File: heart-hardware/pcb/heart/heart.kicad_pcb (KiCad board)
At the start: 4 copper layers, 47.6 x 45.2 mm, 66 parts, among them J1 3V0, J2 DIO, J3 CLK, J5 TOUCH_KEY, SW1 SW_SPDT, U1 STM32L031F6Px, U2 TCA6416APWR, U3 LIS3DH, U4 Holtek-Semicon-BS812A-1

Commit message: Component pacement v1
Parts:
- moved C5 2.13 mm to (42.5, 66.2)
- moved C4 2.12 mm to (42.5, 67.2)
- moved R21 2.10 mm to (42.5, 65.2)
- moved C2 1.97 mm to (57.5, 69.0), turned to 0 degrees
- moved R23 1.45 mm to (57.5, 66.0)
- moved R22 1.33 mm to (57.5, 67.0)
- moved C10 1.25 mm to (54.0, 89.5)
- moved C11 1.23 mm to (46.0, 89.5)
- moved R26 1.10 mm to (54.0, 86.0), turned to 180 degrees
- moved R25 1.00 mm to (54.0, 85.0)
- moved C8 0.90 mm to (46.0, 85.0)
- moved C9 0.90 mm to (46.0, 86.0), turned to 180 degrees
- moved C3 0.53 mm to (57.5, 68.0), turned to 180 degrees
- moved C6 0.35 mm to (57.5, 74.0)
- moved C7 0.33 mm to (57.5, 73.0)

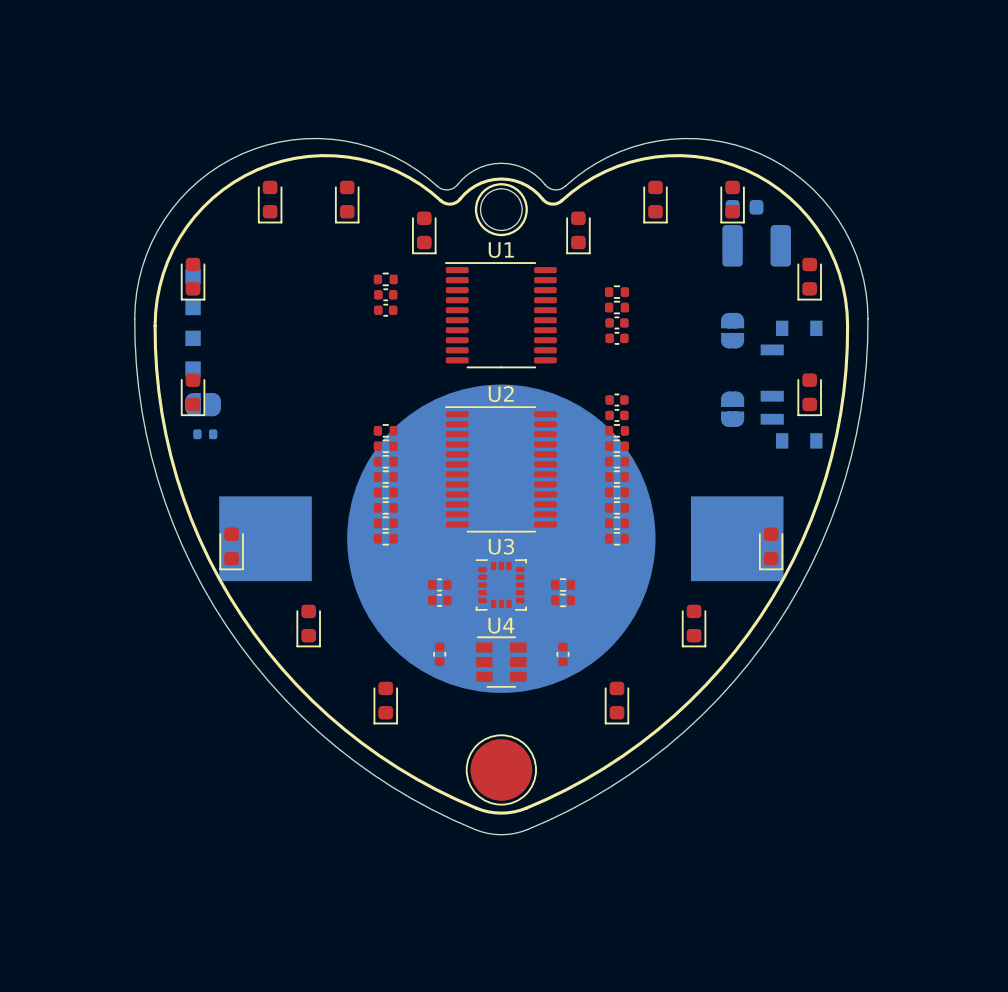
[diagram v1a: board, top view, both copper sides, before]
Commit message: Start routing traces
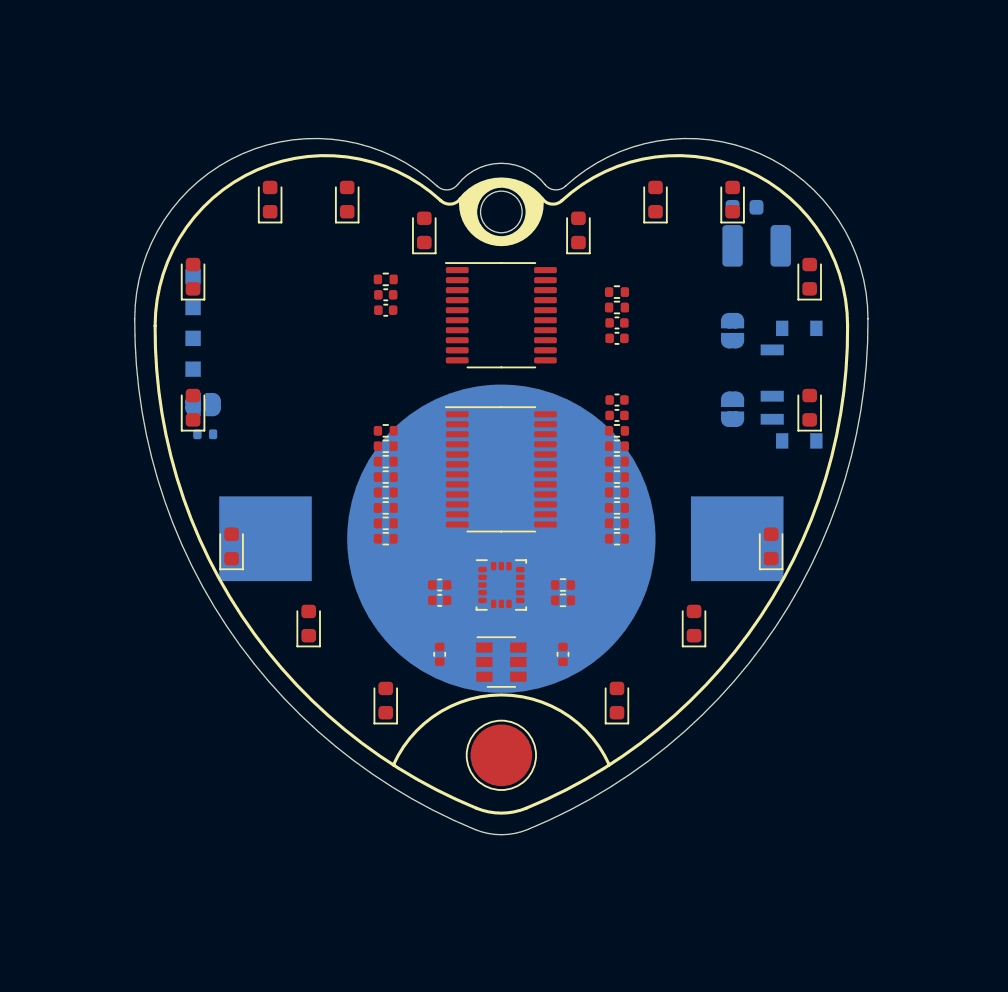
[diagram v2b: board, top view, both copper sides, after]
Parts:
- moved D11 1.00 mm to (70.0, 73.5)
- moved D4 1.00 mm to (30.0, 73.5)
- moved J5 0.95 mm to (50.0, 96.0)
- moved REF** 0.15 mm to (50.0, 60.8)
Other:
- board text removed: "E"
- board text removed: "K"
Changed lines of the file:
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@@
   (general
     (thickness 1.6)
-    (drawings 45)
+    (drawings 42)
     (tracks 0)
     (zones 0)
@@
     (pad_to_mask_clearance 0)
     (aux_axis_origin 0 0)
-    (visible_elements 7FFF7F7F)
+    (visible_elements 7FFEFF1F)
     (pcbplotparams
       (layerselection 0x010fc_ffffffff)
@@
   )
   (module MountingHole:MountingHole_2.7mm (layer F.Cu)
-    (at 50 60.65)
+    (at 50 60.8)
     (descr "Mounting Hole 2.7mm, no annular")
     (tags "mounting hole 2.7mm no annular")
@@
   )
   (module TestPoint:TestPoint_Pad_D4.0mm (layer F.Cu)
-    (at 50 97)
+    (at 50 96.05)
     (descr "SMD pad as test Point, diameter 4.0mm")
     (tags "test point SMD pad")
@@
     (tags SOT-23-6)
     (attr smd)
-    (fp_text reference U4 (at -0.01506 -2.33426) (layer F.SilkS)
+    (fp_text reference U4 (at -0.01506 -2.33426) (layer F.SilkS) hide
       (effects (font (size 1 1) (thickness 0.15)))
     )
@@
   )
   (module LED_SMD:LED_0603_1608Metric (layer F.Cu)
-    (at 30 72.5 90)
+    (at 30 73.5 90)
     (descr "LED SMD 0603 (1608 Metric), square (rectangular) end terminal, IPC_7351 nominal, (Body size source: http://www.tortai-tech.com/upload/download/2011102023233369053.pdf), generated with kicad-footprint-generator")
     (tags LED)
@@
   )
   (module LED_SMD:LED_0603_1608Metric (layer F.Cu)
-    (at 70 72.5 90)
+    (at 70 73.5 90)
     (descr "LED SMD 0603 (1608 Metric), square (rectangular) end terminal, IPC_7351 nominal, (Body size source: http://www.tortai-tech.com/upload/download/2011102023233369053.pdf), generated with kicad-footprint-generator")
     (tags LED)
@@
     (tags "LGA NoLead")
     (attr smd)
-    (fp_text reference U3 (at 0 -2.45) (layer F.SilkS)
+    (fp_text reference U3 (at 0 -2.45) (layer F.SilkS) hide
       (effects (font (size 1 1) (thickness 0.15)))
     )
@@
     (tags "TSSOP SO")
     (attr smd)
-    (fp_text reference U2 (at 0 -4.85) (layer F.SilkS)
+    (fp_text reference U2 (at 0 -4.85) (layer F.SilkS) hide
       (effects (font (size 1 1) (thickness 0.15)))
     )
@@
     (tags "TSSOP SO")
     (attr smd)
-    (fp_text reference U1 (at 0 -4.2) (layer F.SilkS)
+    (fp_text reference U1 (at 0 -4.2) (layer F.SilkS) hide
       (effects (font (size 1 1) (thickness 0.15)))
     )
@@
       ))
   )
-  (gr_text K (at 50.4 98.1) (layer B.SilkS)
-    (effects (font (size 0.75 0.75) (thickness 0.15)) (justify mirror))
-  )
-  (gr_text E (at 49.6 98.1) (layer B.SilkS)
-    (effects (font (size 0.75 0.75) (thickness 0.15)) (justify mirror))
-  )
+  (gr_arc (start 50.006349 60.288693) (end 52.636348 59.968694) (angle 194.5) (layer B.SilkS) (width 0.2))
+  (gr_poly (pts (xy 49.66 58.73) (xy 49.45 58.76) (xy 49.27 58.8) (xy 48.95 58.92) (xy 48.83 58.96) (xy 48.58 59.08) (xy 48.37 59.15) (xy 48.2 59.26) (xy 47.94 59.46) (xy 47.76 59.6) (xy 47.64 59.74) (xy 47.47 59.95) (xy 47.47 60.11) (xy 47.45 60.27) (xy 47.45 60.47) (xy 47.48 60.67) (xy 47.52 60.94) (xy 47.56 61.11) (xy 47.68 61.38) (xy 47.78 61.58) (xy 48 61.9) (xy 48.14 62.06) (xy 48.33 62.25) (xy 48.52 62.38) (xy 48.7 62.5) (xy 48.88 62.63) (xy 49.11 62.72) (xy 49.37 62.8) (xy 49.69 62.86) (xy 50.04 62.88) (xy 50.04 62.5) (xy 49.84 62.47) (xy 49.62 62.42) (xy 49.42 62.35) (xy 49.18 62.26) (xy 49 62.11) (xy 48.86 61.99) (xy 48.69 61.83) (xy 48.5 61.5) (xy 48.4 61.3) (xy 48.35 61.03) (xy 48.36 60.81) (xy 48.39 60.54) (xy 48.4 60.37) (xy 48.49 60.13) (xy 48.59 59.94) (xy 48.9 59.56) (xy 49.15 59.4) (xy 49.34 59.27) (xy 49.61 59.18) (xy 49.81 59.14) (xy 50.04 59.14) (xy 50.04 58.71) (xy 49.78 58.71)) (layer B.SilkS) (width 0.1))
+  (gr_poly (pts (xy 50.04 59.15) (xy 50.24 59.17) (xy 50.48 59.22) (xy 50.75 59.34) (xy 51.04 59.52) (xy 51.32 59.77) (xy 51.46 59.99) (xy 51.6 60.3) (xy 51.65 60.52) (xy 51.68 60.79) (xy 51.66 61.1) (xy 51.57 61.48) (xy 51.42 61.7) (xy 51.22 61.98) (xy 51.02 62.14) (xy 50.77 62.29) (xy 50.5 62.4) (xy 50.23 62.48) (xy 50.14 62.49) (xy 50.04 62.49) (xy 50.04 62.87) (xy 50.5 62.85) (xy 51.1 62.65) (xy 51.79 62.21) (xy 52.3 61.59) (xy 52.62 60.85) (xy 52.65 60.31) (xy 52.65 60.03) (xy 52.58 59.86) (xy 52.2 59.49) (xy 51.91 59.29) (xy 51.62 59.12) (xy 51.1 58.88) (xy 50.71 58.78) (xy 50.22 58.73) (xy 50.04 58.73)) (layer B.SilkS) (width 0.1))
+  (gr_poly (pts (xy 50.38 58.72) (xy 50.59 58.75) (xy 50.77 58.79) (xy 51.09 58.91) (xy 51.21 58.95) (xy 51.46 59.07) (xy 51.67 59.14) (xy 51.84 59.25) (xy 52.1 59.45) (xy 52.28 59.59) (xy 52.4 59.73) (xy 52.57 59.94) (xy 52.57 60.1) (xy 52.59 60.26) (xy 52.59 60.46) (xy 52.56 60.66) (xy 52.52 60.93) (xy 52.48 61.1) (xy 52.36 61.37) (xy 52.26 61.57) (xy 52.04 61.89) (xy 51.9 62.05) (xy 51.71 62.24) (xy 51.52 62.37) (xy 51.34 62.49) (xy 51.16 62.62) (xy 50.93 62.71) (xy 50.67 62.79) (xy 50.35 62.85) (xy 50 62.87) (xy 50 62.49) (xy 50.2 62.46) (xy 50.42 62.41) (xy 50.62 62.34) (xy 50.86 62.25) (xy 51.04 62.1) (xy 51.18 61.98) (xy 51.35 61.82) (xy 51.54 61.49) (xy 51.64 61.29) (xy 51.69 61.02) (xy 51.68 60.8) (xy 51.65 60.53) (xy 51.64 60.36) (xy 51.55 60.12) (xy 51.45 59.93) (xy 51.14 59.55) (xy 50.89 59.39) (xy 50.7 59.26) (xy 50.43 59.17) (xy 50.23 59.13) (xy 50 59.13) (xy 50 58.7) (xy 50.26 58.7)) (layer F.SilkS) (width 0.1))
+  (gr_poly (pts (xy 50 59.14) (xy 49.8 59.16) (xy 49.56 59.21) (xy 49.29 59.33) (xy 49 59.51) (xy 48.72 59.76) (xy 48.58 59.98) (xy 48.44 60.29) (xy 48.39 60.51) (xy 48.36 60.78) (xy 48.38 61.09) (xy 48.47 61.47) (xy 48.62 61.69) (xy 48.82 61.97) (xy 49.02 62.13) (xy 49.27 62.28) (xy 49.54 62.39) (xy 49.81 62.47) (xy 49.9 62.48) (xy 50 62.48) (xy 50 62.86) (xy 49.54 62.84) (xy 48.94 62.64) (xy 48.25 62.2) (xy 47.74 61.58) (xy 47.42 60.84) (xy 47.39 60.3) (xy 47.39 60.02) (xy 47.46 59.85) (xy 47.84 59.48) (xy 48.13 59.28) (xy 48.42 59.11) (xy 48.94 58.87) (xy 49.33 58.77) (xy 49.82 58.72) (xy 50 58.72)) (layer F.SilkS) (width 0.1))
+  (gr_arc (start 50 60.27) (end 47.370001 59.950001) (angle -194.5) (layer F.SilkS) (width 0.2))
+  (gr_arc (start 50 99.8) (end 56.999999 96.670001) (angle -131.9) (layer F.SilkS) (width 0.2))
   (gr_text "" (at 55.801868 105.003514) (layer B.SilkS)
     (effects (font (size 0.241681 0.217512) (thickness 0.03021)) (justify left top))
   )
-  (gr_arc (start 50.167347 97.297176) (end 50.133877 97.323369) (angle -94.62084646) (layer B.SilkS) (width 0.125))
-  (gr_arc (start 50 97.428139) (end 50.133877 97.323369) (angle -103.90789) (layer B.SilkS) (width 0.125))
-  (gr_arc (start 49.832652 97.297176) (end 49.803849 97.328427) (angle -94.62084646) (layer B.SilkS) (width 0.125))
-  (gr_arc (start 49.4294 97.734684) (end 49.803849 97.328427) (angle -132.6669014) (layer B.SilkS) (width 0.125))
-  (gr_arc (start 50.556385 97.745099) (end 48.8769 97.734684) (angle -68.06729905) (layer B.SilkS) (width 0.125))
-  (gr_arc (start 50 99.102514) (end 49.919406 99.299138) (angle -44.57606982) (layer B.SilkS) (width 0.125))
-  (gr_arc (start 49.443614 97.745099) (end 50.080593 99.299138) (angle -68.06729905) (layer B.SilkS) (width 0.125))
-  (gr_arc (start 50.570599 97.734684) (end 51.123099 97.734684) (angle -132.6669014) (layer B.SilkS) (width 0.125))
   (gr_text "" (at 15.601868 65.278514) (layer B.SilkS)
     (effects (font (size 0.241681 0.217512) (thickness 0.03021)) (justify left top))
   )
-  (gr_circle (center 50.005122 60.65) (end 51.505122 61.325) (layer B.SilkS) (width 0.15))
-  (gr_circle (center 50 60.65) (end 51.5 59.975) (layer F.SilkS) (width 0.15))
+  (gr_circle (center 50.005122 60.8) (end 51.505122 61.475) (layer B.SilkS) (width 0.15))
+  (gr_circle (center 50 60.8) (end 51.5 60.125) (layer F.SilkS) (width 0.15))
   (gr_line (start 50 50) (end 50 150) (layer Dwgs.User) (width 0.15))
   (gr_text "" (at 27.537365 108.070283) (layer F.SilkS)
